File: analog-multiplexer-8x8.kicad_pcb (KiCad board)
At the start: 2 copper layers, 60.6 x 92.7 mm, 30 parts, among them J1 Conn_01x13, J2 Conn_02x08_Odd_Even, U1 4051, U2 4051, U3 4051, U4 4051, U5 4051, U6 4051, U7 4051, U8 4051

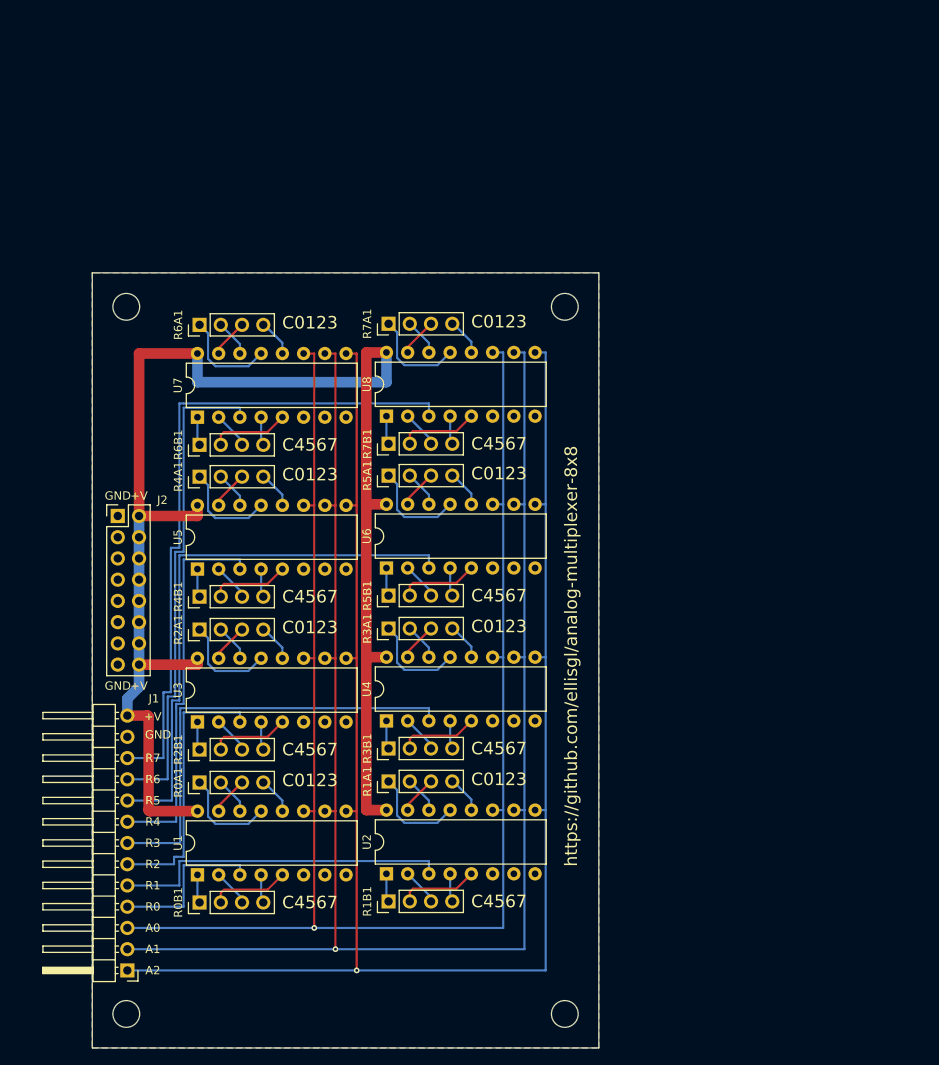
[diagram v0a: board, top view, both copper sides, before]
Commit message: Replace KiCad 5 project with updated KiCad project
Remove the old schematic, netlist, PDF and Gerber plots, and add the
new .kicad_pro/.kicad_sch/.kicad_pcb files and a board render. Keep
LICENSE.BSD and README.md.

Co-Authored-By: Claude Opus 5.5 <noreply@anthropic.com>
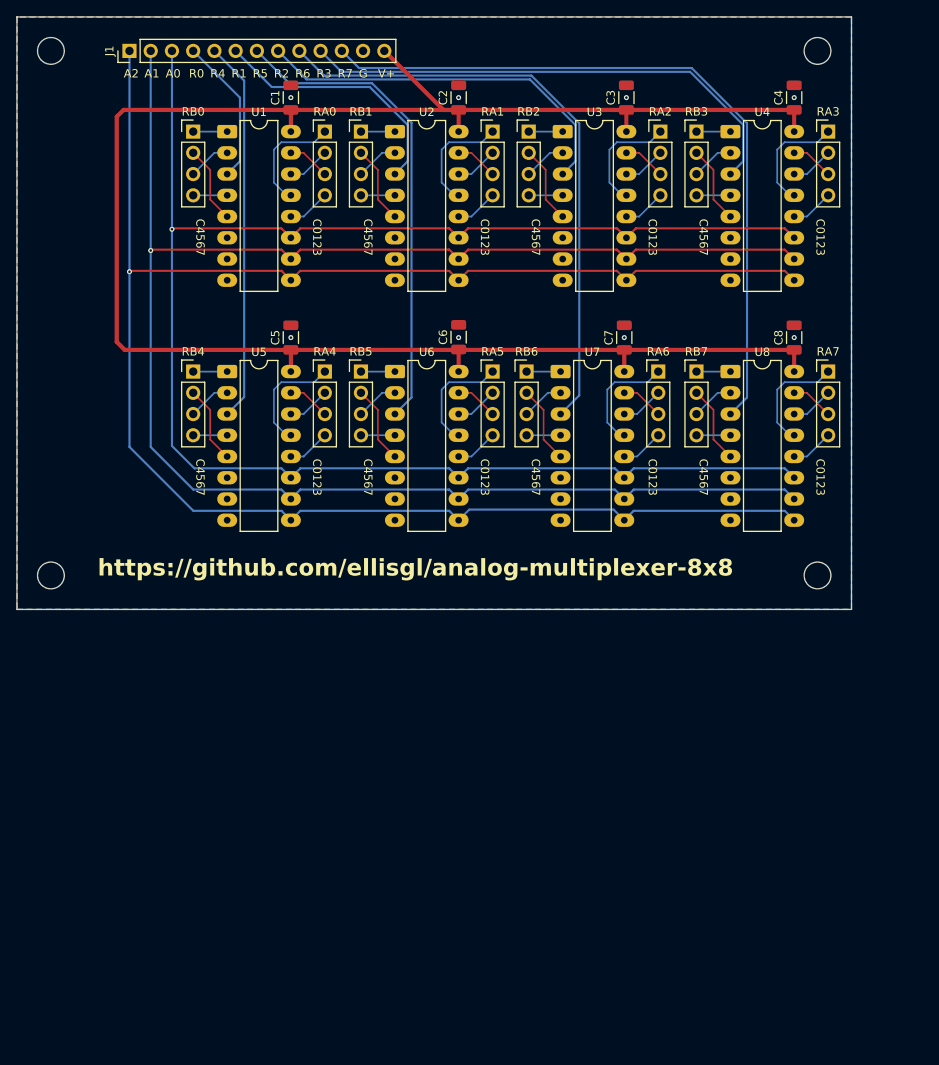
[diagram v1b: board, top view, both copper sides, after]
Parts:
- removed ? (x4): MountingHole_3.2mm_M3, Mounting_Holes:MountingHole_3.2mm_M3
- removed J2: Conn_02x08_Odd_Even, Pin_Headers:Pin_Header_Straight_2x08_Pitch2.54mm
- removed R0A1, R0B1, R1A1, R1B1, R2A1, R2B1, R3A1, R3B1, R4A1, R4B1, R5A1, R5B1, R6A1, R6B1, R7A1, R7B1: Conn_01x04, Pin_Headers:Pin_Header_Straight_1x04_Pitch2.54mm
- added C1: 100nf, Capacitor_SMD:C_1206_3216Metric, F.Cu at (48.0, 24.9)
- added C2: 100nf, Capacitor_SMD:C_1206_3216Metric, F.Cu at (68.1, 24.9)
- added C3: 100nf, Capacitor_SMD:C_1206_3216Metric, F.Cu at (88.1, 24.9)
- added C4: 100nf, Capacitor_SMD:C_1206_3216Metric, F.Cu at (108.2, 24.9)
- added C5: 100nf, Capacitor_SMD:C_1206_3216Metric, F.Cu at (48.0, 53.6)
- added C6: 100nf, Capacitor_SMD:C_1206_3216Metric, F.Cu at (68.1, 53.5)
- added C7: 100nf, Capacitor_SMD:C_1206_3216Metric, F.Cu at (87.9, 53.6)
- added C8: 100nf, Capacitor_SMD:C_1206_3216Metric, F.Cu at (108.2, 53.6)
- added RA0: Conn_01x04, Connector_PinHeader_2.54mm:PinHeader_1x04_P2.54mm_Vertical, F.Cu at (52.1, 29.0)
- added RA1: Conn_01x04, Connector_PinHeader_2.54mm:PinHeader_1x04_P2.54mm_Vertical, F.Cu at (72.1, 29.0)
- added RA2: Conn_01x04, Connector_PinHeader_2.54mm:PinHeader_1x04_P2.54mm_Vertical, F.Cu at (92.2, 29.0)
- added RA3: Conn_01x04, Connector_PinHeader_2.54mm:PinHeader_1x04_P2.54mm_Vertical, F.Cu at (112.3, 29.0)
- added RA4: Conn_01x04, Connector_PinHeader_2.54mm:PinHeader_1x04_P2.54mm_Vertical, F.Cu at (52.1, 57.7)
- added RA5: Conn_01x04, Connector_PinHeader_2.54mm:PinHeader_1x04_P2.54mm_Vertical, F.Cu at (72.1, 57.7)
- added RA6: Conn_01x04, Connector_PinHeader_2.54mm:PinHeader_1x04_P2.54mm_Vertical, F.Cu at (91.9, 57.7)
- added RA7: Conn_01x04, Connector_PinHeader_2.54mm:PinHeader_1x04_P2.54mm_Vertical, F.Cu at (112.3, 57.7)
- added RB0: Conn_01x04, Connector_PinHeader_2.54mm:PinHeader_1x04_P2.54mm_Vertical, F.Cu at (36.3, 29.0)
- added RB1: Conn_01x04, Connector_PinHeader_2.54mm:PinHeader_1x04_P2.54mm_Vertical, F.Cu at (56.4, 29.0)
- added RB2: Conn_01x04, Connector_PinHeader_2.54mm:PinHeader_1x04_P2.54mm_Vertical, F.Cu at (76.5, 29.0)
- added RB3: Conn_01x04, Connector_PinHeader_2.54mm:PinHeader_1x04_P2.54mm_Vertical, F.Cu at (96.5, 29.0)
- added RB4: Conn_01x04, Connector_PinHeader_2.54mm:PinHeader_1x04_P2.54mm_Vertical, F.Cu at (36.3, 57.7)
- added RB5: Conn_01x04, Connector_PinHeader_2.54mm:PinHeader_1x04_P2.54mm_Vertical, F.Cu at (56.4, 57.7)
- added RB6: Conn_01x04, Connector_PinHeader_2.54mm:PinHeader_1x04_P2.54mm_Vertical, F.Cu at (76.2, 57.7)
- added RB7: Conn_01x04, Connector_PinHeader_2.54mm:PinHeader_1x04_P2.54mm_Vertical, F.Cu at (96.5, 57.7)
- added REF**: MountingHole_3.2mm_M3, MountingHole:MountingHole_3.2mm_M3, F.Cu at (111.0, 82.0)
- added REF**: MountingHole_3.2mm_M3, MountingHole:MountingHole_3.2mm_M3, F.Cu at (111.0, 19.3)
- added REF**: MountingHole_3.2mm_M3, MountingHole:MountingHole_3.2mm_M3, F.Cu at (19.3, 19.3)
- added REF**: MountingHole_3.2mm_M3, MountingHole:MountingHole_3.2mm_M3, F.Cu at (19.3, 82.0)
- J1: footprint Pin_Headers:Pin_Header_Angled_1x13_Pitch2.54mm -> Connector_PinHeader_2.54mm:PinHeader_1x13_P2.54mm_Vertical
- U1, U2, U3, U4, U5, U6, U7, U8: value 4051 -> 74HCT4051; footprint Housings_DIP:DIP-16_W7.62mm -> Package_DIP:DIP-16_W7.62mm_LongPads
- moved J1 110.0 mm to (28.7, 19.3), turned to 90 degrees
- moved U1 89.0 mm to (40.4, 29.0), turned to 0 degrees
- moved U2 88.8 mm to (60.5, 29.0), turned to 0 degrees
- moved U3 83.0 mm to (80.5, 29.0), turned to 0 degrees
- moved U4 81.6 mm to (100.6, 29.0), turned to 0 degrees
- moved U7 43.8 mm to (80.3, 57.7), turned to 0 degrees
- moved U8 41.5 mm to (100.6, 57.7), turned to 0 degrees
- moved U5 23.9 mm to (40.4, 57.7), turned to 0 degrees
- moved U6 23.5 mm to (60.5, 57.7), turned to 0 degrees
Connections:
- J1 pad 10: R6 -> R3
- J1 pad 5: R1 -> R4
- J1 pad 6: R2 -> R1
- J1 pad 7: R3 -> R5
- J1 pad 8: R4 -> R2
- J1 pad 9: R5 -> R6
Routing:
- net VCC: track 181.3 -> 222.5 mm
- net R6: track 59.0 -> 72.8 mm
- net R2: track 32.8 -> 45.7 mm
- net A0: track 192.7 -> 203.8 mm
- net R1: track 40.5 -> 30.8 mm
- net A1: track 200.3 -> 210.0 mm
- net R5: track 66.9 -> 57.7 mm
- net Net-(RA5-Pin_1): track 21.5 -> 13.1 mm
- net Net-(RA6-Pin_1): track 21.5 -> 13.1 mm
- net Net-(RA4-Pin_1): track 21.5 -> 13.1 mm
- net Net-(RA3-Pin_1): track 21.5 -> 13.1 mm
- net Net-(RA1-Pin_1): track 21.5 -> 13.1 mm
- net Net-(RA7-Pin_1): track 21.5 -> 13.1 mm
- net Net-(RA2-Pin_1): track 21.5 -> 13.1 mm
- net A2: track 207.9 -> 216.2 mm
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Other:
- board size 60.6 x 92.7 mm -> 99.8 x 70.9 mm
- net class Default removed
- rule pad_to_mask_clearance: 0.0508 -> 0
- board text added: "G"
- board text added: "V+"
- board text removed: "+V"
- board text removed: "GND"
